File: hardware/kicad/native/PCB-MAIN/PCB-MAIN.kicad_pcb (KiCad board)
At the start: 6 copper layers, 110 x 75 mm, 251 parts, among them J10 U.FL-R-SMT-1(60), J11 USB4105-GF-A-120, J12 MEM2052-00-195-00-A, J13 504050-0291, J6 2336582-1, J7 2336582-1, J8 U.FL-R-SMT-1(60), J9 U.FL-R-SMT-1(60), Q1 MMBT3904,215, Q2 MMBT3904,215, Q3 MMBT3904,215, Q4 Si1016X-T1-GE3, U1 STM32U585VIT6Q, U10 E22-900M22S, U11 MDBT50Q-P1MV2, U13 TS3A27518EPWR, U14 ESDALC6V1-5P6, U15 ESDALC6V1-5P6, U16 SN74AXC8T245PWR, U17 SN74LVC32APWR, U18 SN74AXC1T45DRLR, U19 TPD4E05U06DQAR, U2 W25Q512JVFIQ, U20 TPD4E05U06DQAR, U21 TPD4E05U06DQAR, U22 TPD4E05U06DQAR, U23 TPD4E05U06DQAR, U24 TPD4E05U06DQAR, U25 TPD2EUSB30DRTR, U26 TPD2EUSB30DRTR, U27 TPD4E05U06DQAR, U3 LIS2DW12TR, U4 STTS22HTR, U5 LT6000IDCB#TRMPBF, U6 SN74LVC1G07DBVR, U7 SN74AXC8T245PWR, U8 BG95-M3, U9 MAX-M10S-00B, X1 SiT1552AI-JE-DCC-32.768D

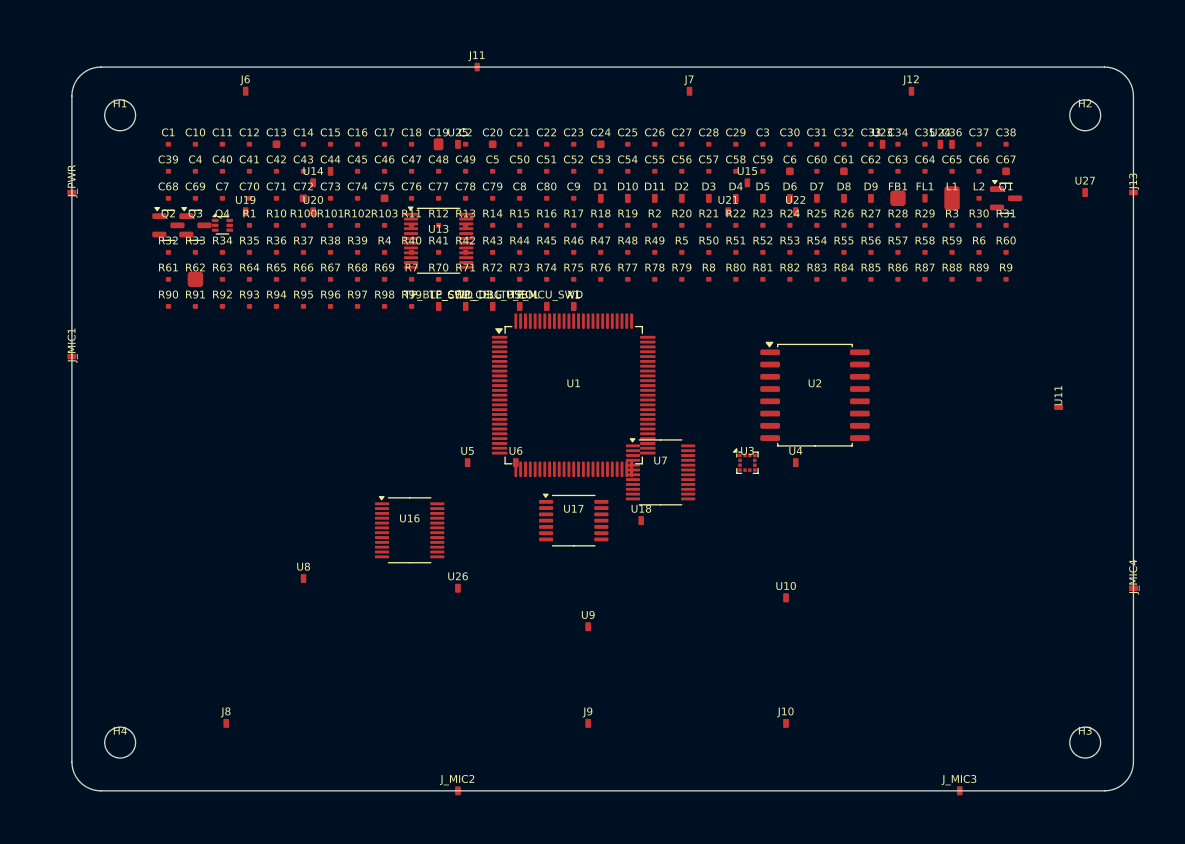
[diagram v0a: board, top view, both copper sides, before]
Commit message: pcb(main): qualify standard footprint candidates
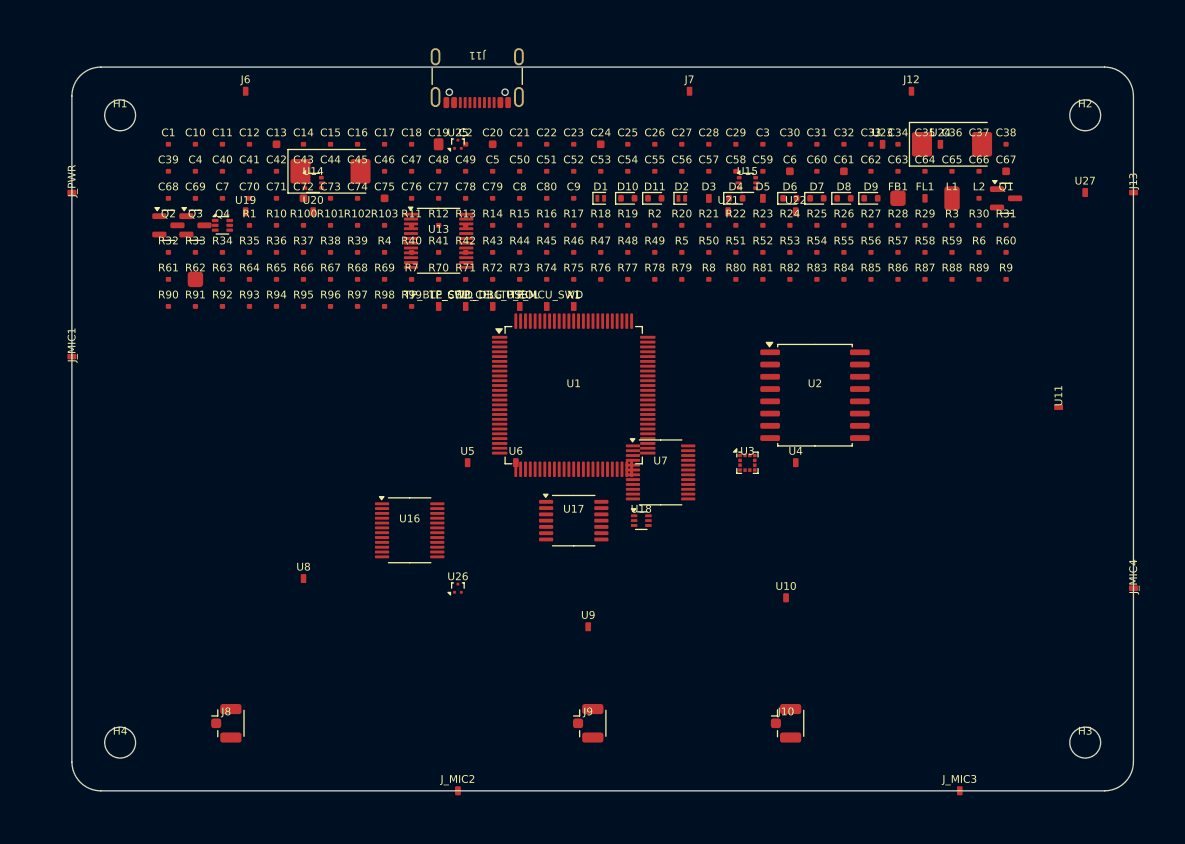
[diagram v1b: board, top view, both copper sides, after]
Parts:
- C36, C44: footprint (none) -> CP_EIA-7343-31_Kemet-D
- D1, D2: footprint (none) -> D_SOD-882
- D10, D11, D4, D6, D7, D8, D9: footprint (none) -> D_SOD-523
- J10, J8, J9: footprint (none) -> U.FL_Hirose_U.FL-R-SMT-1_Vertical
- J11: footprint (none) -> USB_C_Receptacle_GCT_USB4105-xx-A_16P_TopMnt_Horizontal
- U14, U15: footprint (none) -> SOT-666
- U18: footprint (none) -> Texas_R-PDSO-N6_DRL-6
- U25, U26: footprint (none) -> Texas_DRT-3

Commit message: pcb(main): control pogo geometry and footprint placement
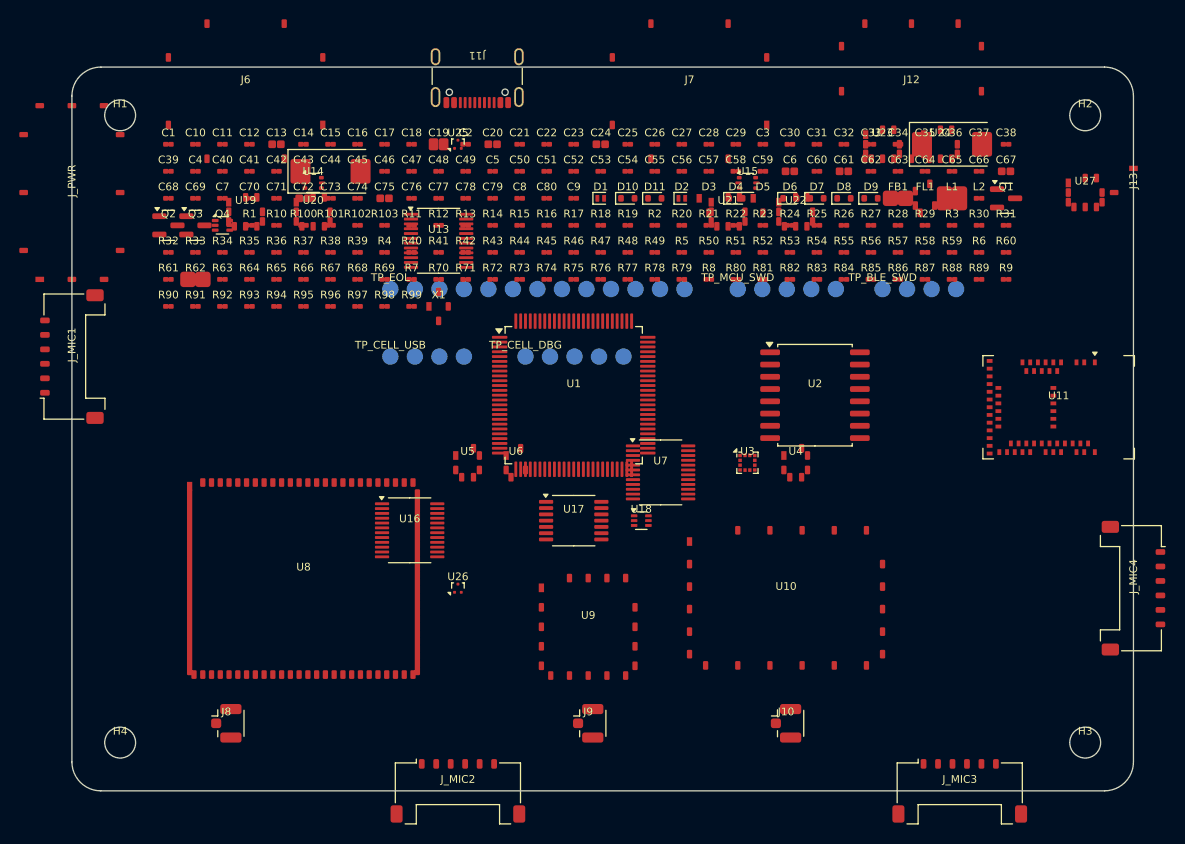
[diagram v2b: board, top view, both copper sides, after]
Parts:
- J_MIC1, J_MIC2, J_MIC3, J_MIC4: footprint (none) -> Molex_Pico-Lock_504050-0691_1x06-1MP_P1.50mm_Horizontal
- TP_BLE_SWD, TP_CELL_DBG, TP_CELL_USB, TP_EOL, TP_MCU_SWD: moved to B.Cu
- U11: footprint (none) -> Raytac_MDBT50Q
- moved TP_BLE_SWD 46.0 mm to (84.0, 23.0)
- moved TP_MCU_SWD 19.9 mm to (69.0, 23.0)
- moved X1 14.0 mm to (38.0, 24.8)
- moved TP_EOL 13.5 mm to (33.0, 23.0)
- moved TP_CELL_USB 11.8 mm to (33.0, 30.0)
- moved TP_CELL_DBG 8.09 mm to (47.0, 30.0)

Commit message: pcb(main): qualify TI DQA and DBV land patterns
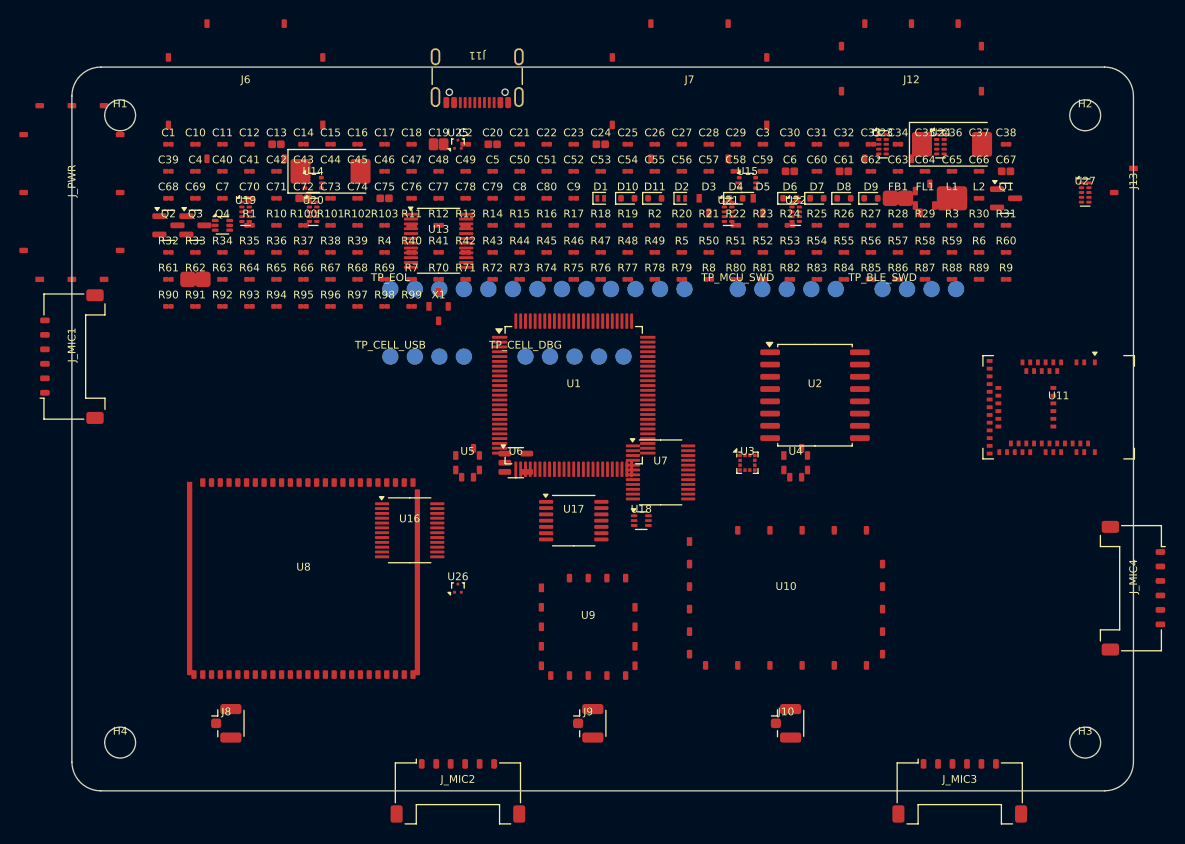
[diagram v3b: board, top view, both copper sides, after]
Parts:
- U19, U20, U21, U22, U23, U24, U27: footprint (none) -> USON-10_2.5x1.0mm_P0.5mm
- U6: footprint (none) -> SOT-23-5

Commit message: pcb(main): add controlled Nexperia SOD962 pattern
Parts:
- D3, D5: footprint (none) -> PESD5V0C1BSF_SOD962-2

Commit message: pcb(main): control STTS22H and LT6000 land patterns
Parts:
- U4: footprint (none) -> STTS22H_UDFN-6L
- U5: footprint (none) -> LT6000_DCB-7

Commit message: pcb(main): control SiT1552 JE land pattern
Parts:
- X1: footprint (none) -> SiT1552_JE_CSP-4

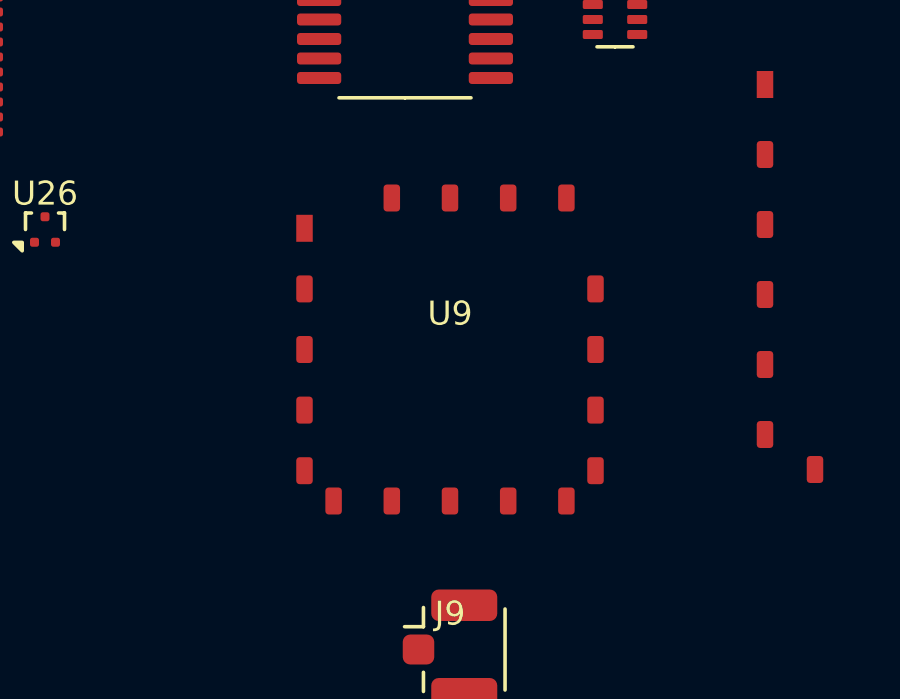
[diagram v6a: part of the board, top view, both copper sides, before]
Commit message: pcb(main): control MAX-M10S copper land pattern
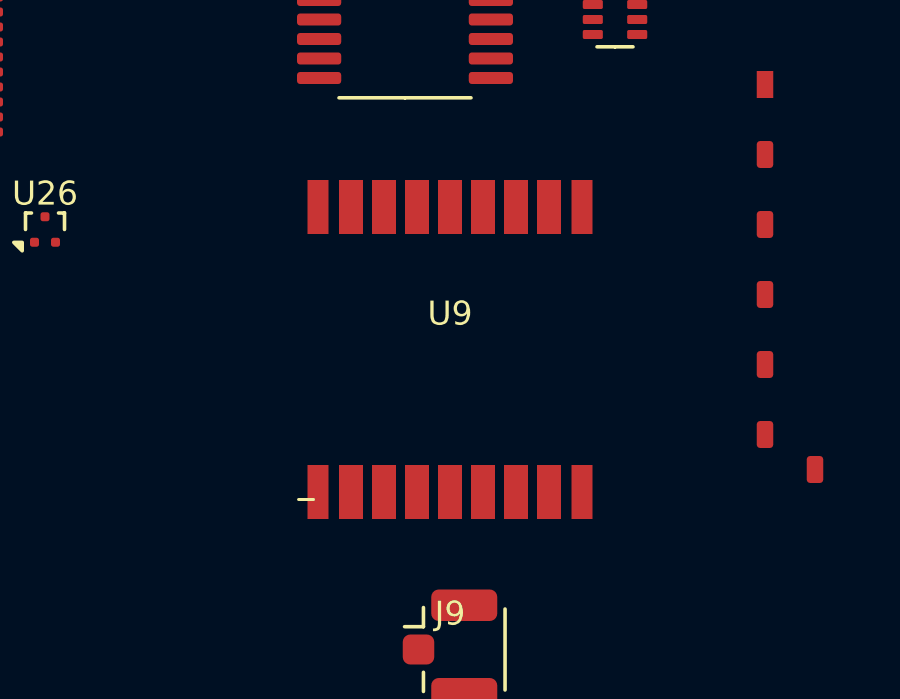
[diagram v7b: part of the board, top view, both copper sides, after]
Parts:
- U9: footprint (none) -> u-blox_MAX-M10S_LCC-18

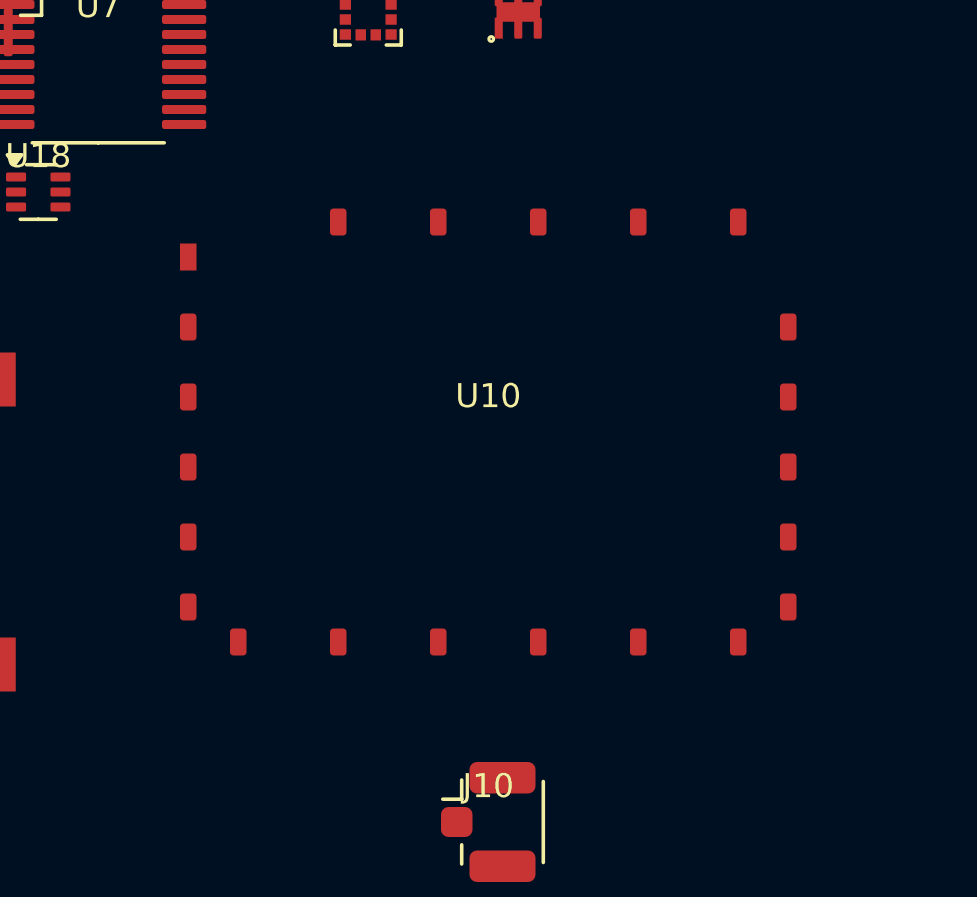
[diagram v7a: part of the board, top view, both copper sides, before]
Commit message: pcb(main): control E22-M22S castellated land pattern
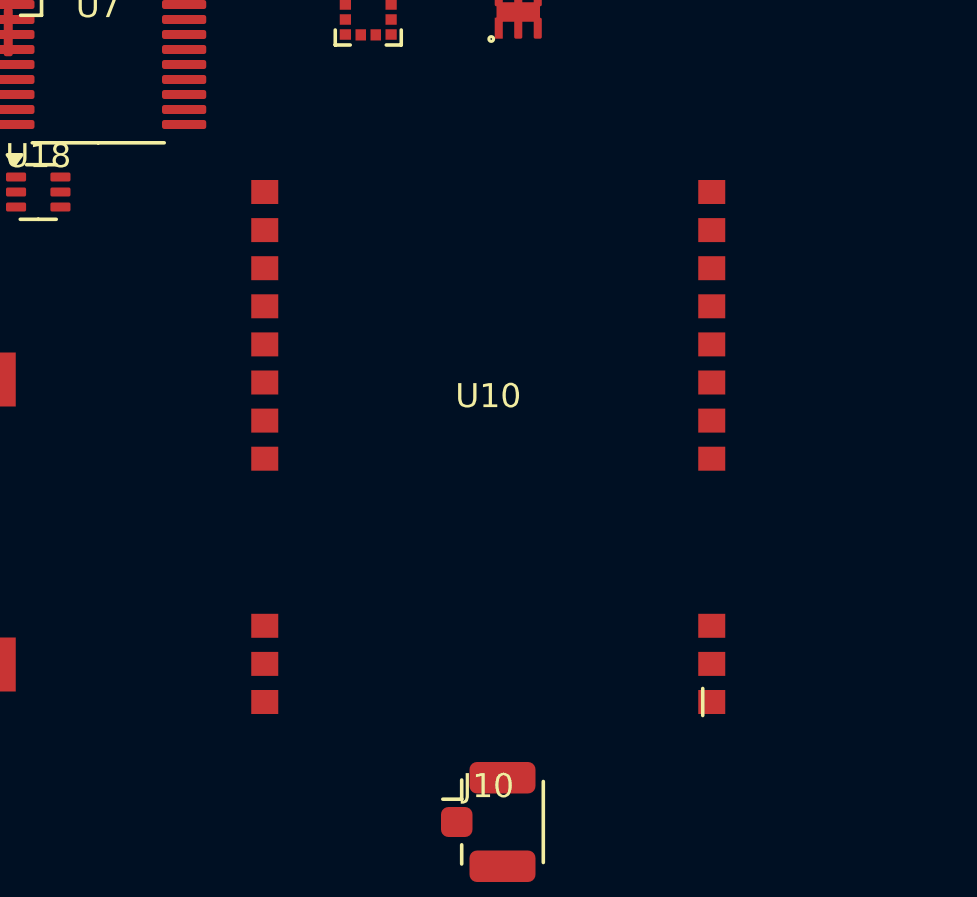
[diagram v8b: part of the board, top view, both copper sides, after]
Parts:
- U10: footprint (none) -> Ebyte_E22-M22S_Castellated-22
